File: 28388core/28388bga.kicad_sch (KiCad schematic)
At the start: 130 parts, among them IC1 F28388DZWTS, IC2 TPS62420DRCT, IC6 OPA4350EA_250, IC7 TPS3702CX33DDCT, IC8 CDCLVC1104PW, IC9 TPS3702CX12DDCT, J9 Conn_02x07_Odd_Even, Q1 FMMT618TA, Q11 AT24C16C-SSHM-T, Q2 FMMT618TA, Q4 FMMT618TA, Q46 TYPEC-304-ACP16, Q7 FMMT618TA, SW1 SW_DIP_x02, SW2 SW_Push, U1 ADR423ARMZ, Y1 ECS-2520S33-250-FN-TR

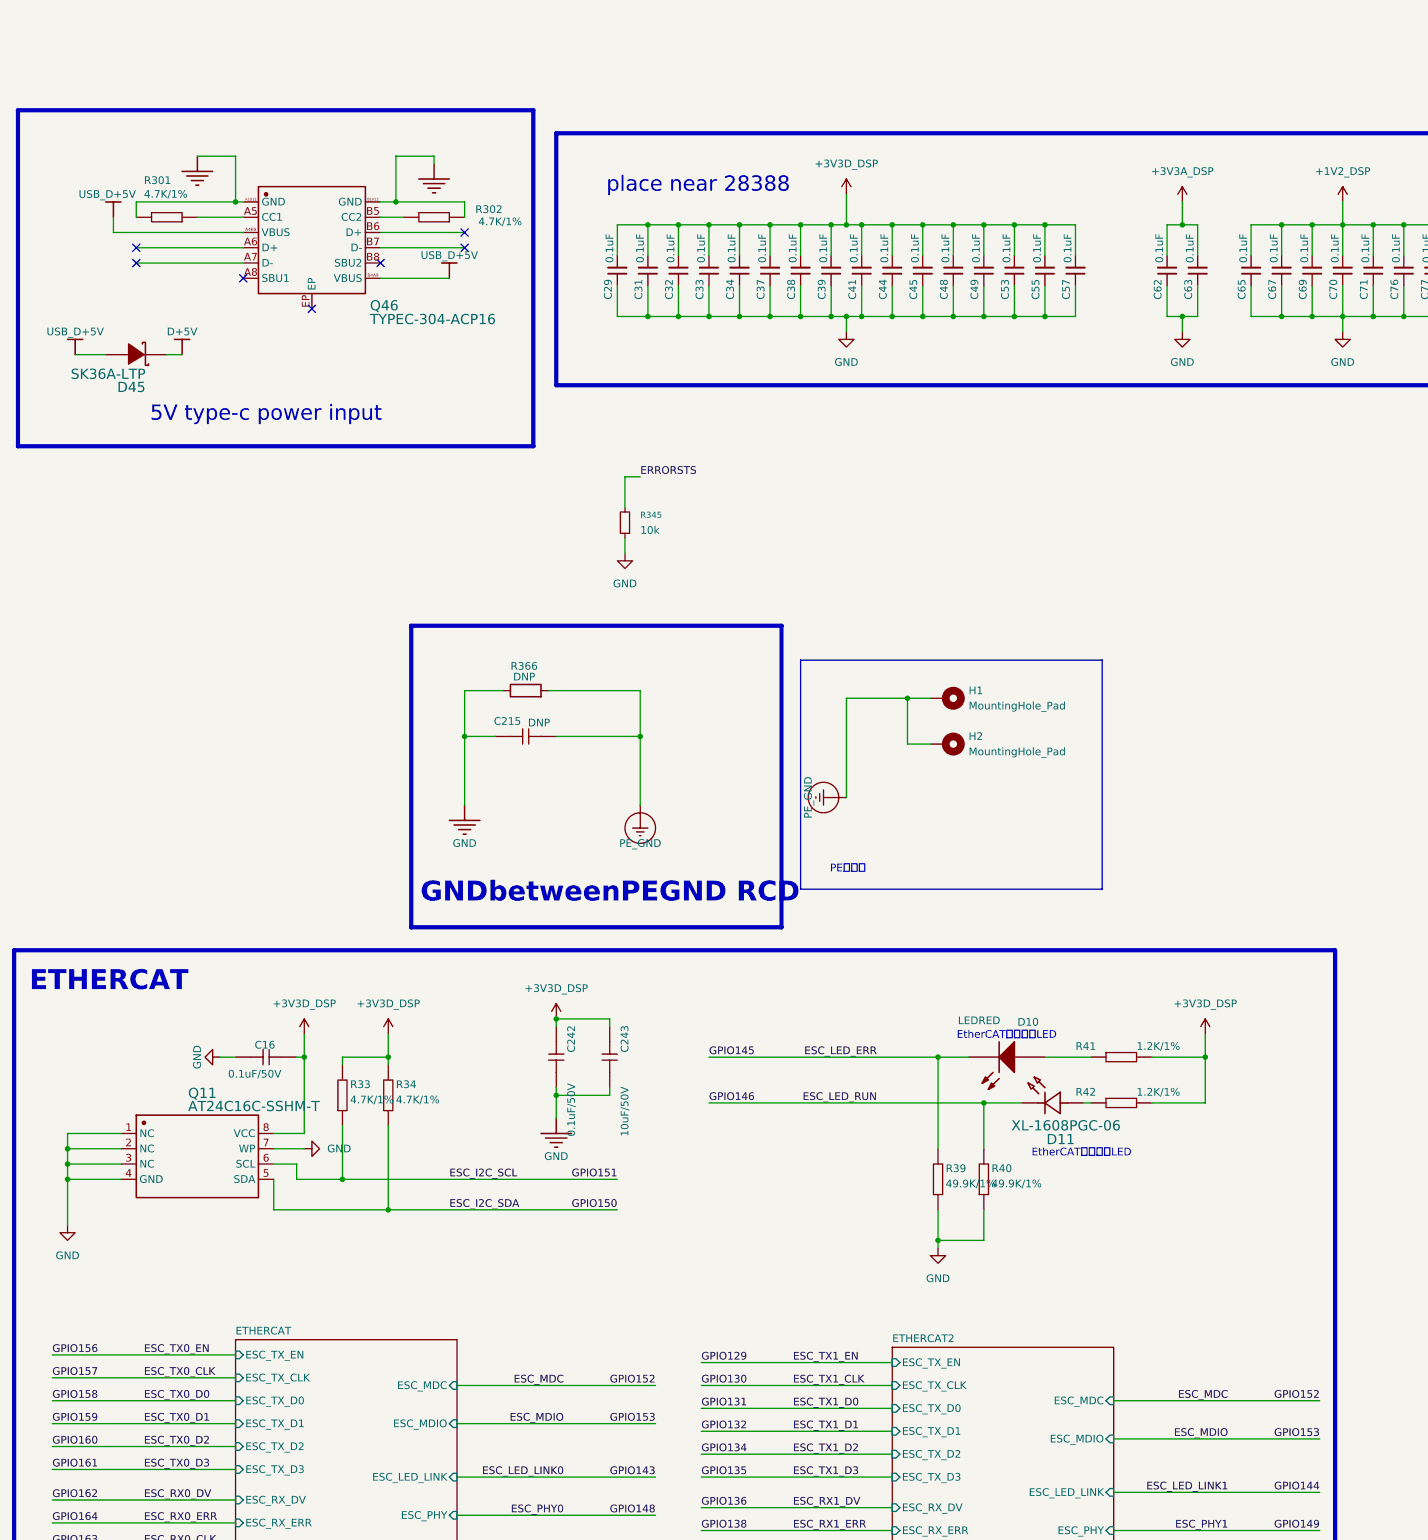
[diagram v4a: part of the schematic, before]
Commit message: 1. usb 稳压、防倒灌 1 2. 仿真器贴片 1 3. EtherCAT确认 1 4. EtherCAT差分信号 5. 金手指选型换1.6 要不就1.0？
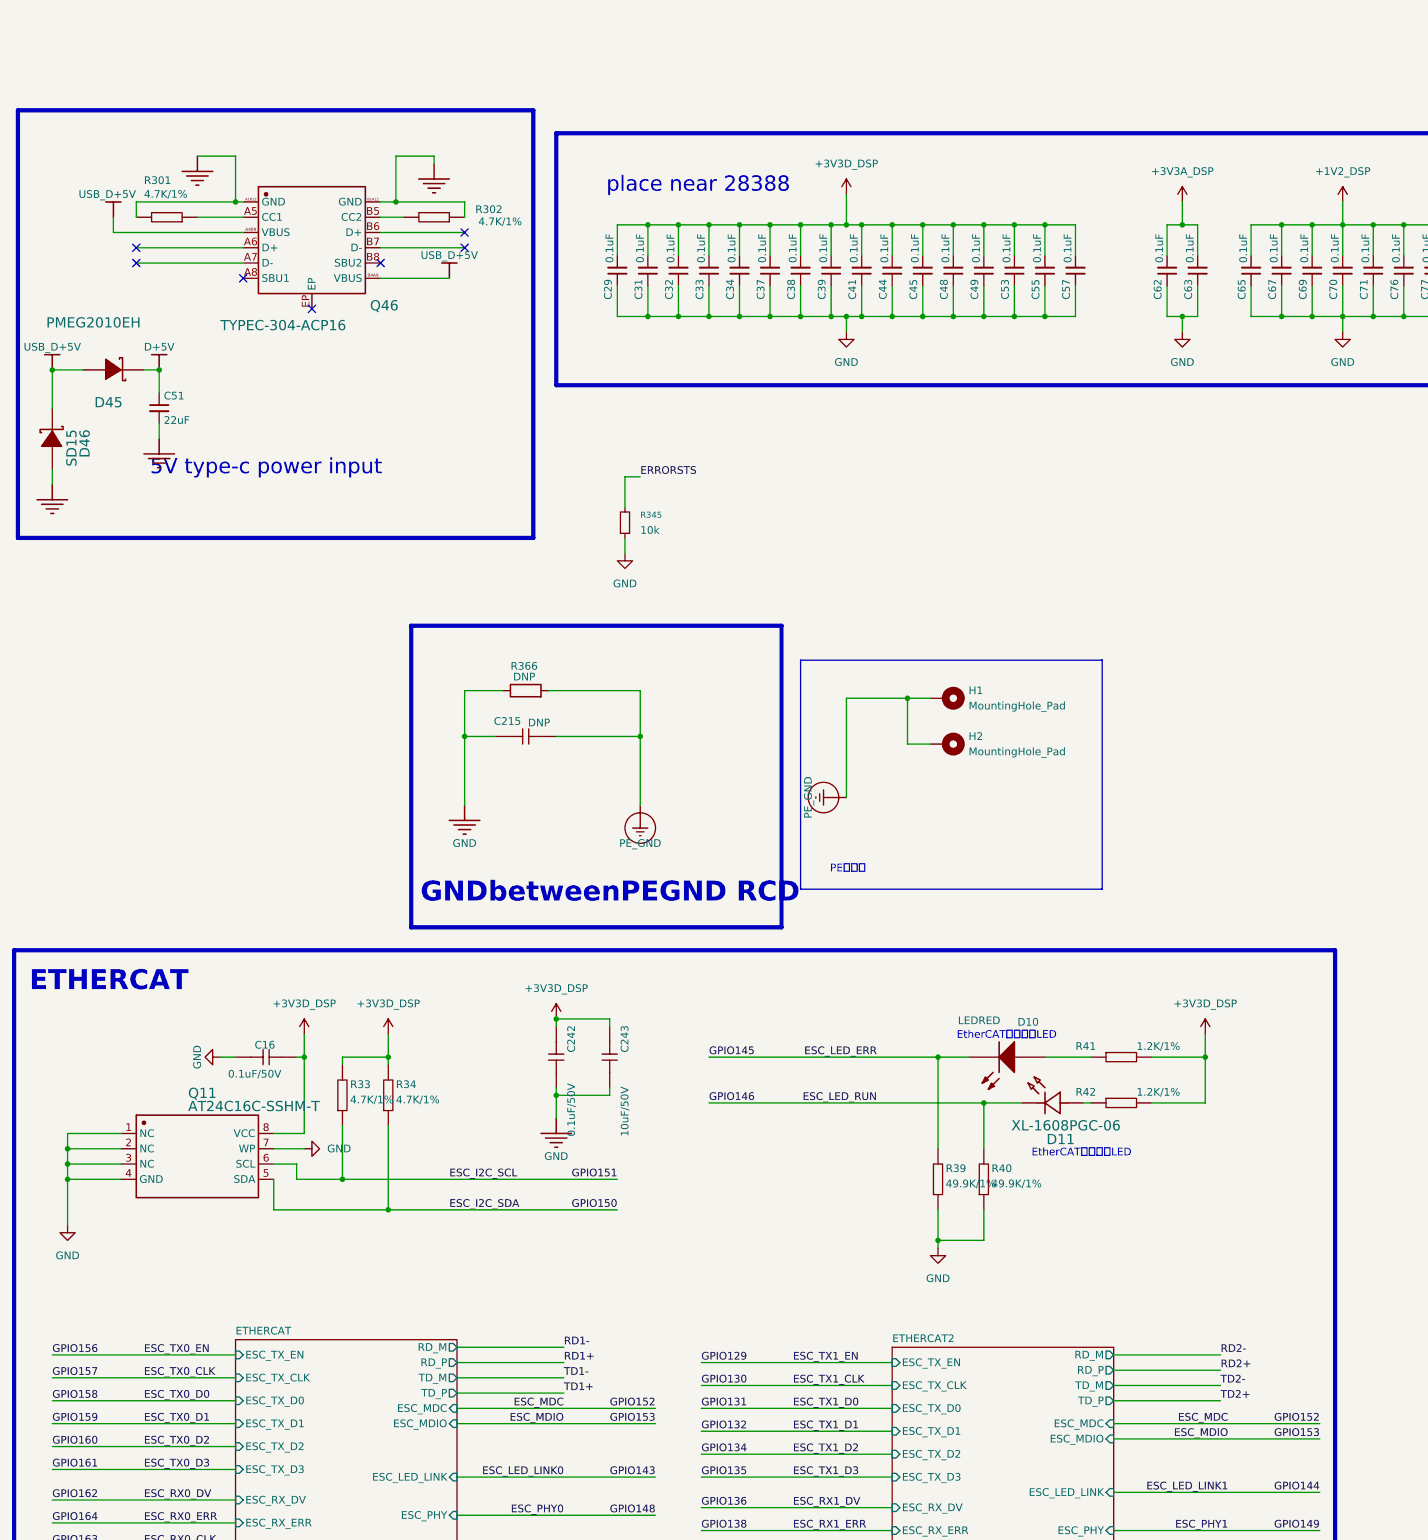
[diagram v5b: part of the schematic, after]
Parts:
- added C51: 22uF, Capacitor_SMD:C_0402_1005Metric, symbol Device:C_Small
- added D46: SD15, Diode_SMD:D_SOD-323, symbol sheet1-altium-import:SK36A-LTP
- D45: value SK36A-LTP -> PMEG2010EH; footprint Lib_sheet_10:SMA_L4.3-W2.6-LS5.2-RD -> Diode_SMD:D_SOD-123F; Manufacturer MCC(美微科) -> (none); Manufacturer Part SK36A-LTP -> (none); Supplier Part C106867 -> C552825
- J9: footprint Connector_IDC:IDC-Header_2x07_P2.54mm_Vertical -> Connector_PinHeader_2.54mm:PinHeader_2x07_P2.54mm_Vertical_SMD
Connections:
- net AGND: now also C51.2, D46.2 (A)
- net D+5V: now also C51.1
- net USB_D+5V: now also D46.1 (K)
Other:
- sheet ETHERCAT ports: added RD_M, RD_P, TD_M, TD_P; removed none
- sheet ETHERCAT2 ports: added RD_M, RD_P, TD_M, TD_P; removed none
- moved on the sheet: D45

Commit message: 使用100PIN连接器，试着重新分配引脚
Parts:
- removed CARD2: DDR3, 1mmlab_footprint:PCBComponent_1 - duplicate, symbol 1mmlab:DDR3
- added CN1, CN2: ~, 1mmlab_footprint:CONN-SMD_DF40C-100DS-0.4V-51, symbol 1mmlab:DF40C-100DS-0.4V(51)
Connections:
- net ADC_14_IN: now also CN1.90
- net ADC_15_IN: now also CN1.89
- net ADC_A0_IN: now also CN1.2
- net ADC_A1_IN: now also CN1.3
- net ADC_A2_IN: now also CN1.5
- net ADC_A3_IN: now also CN1.6
- net ADC_A4_IN: now also CN1.8
- net ADC_A5_IN: now also CN1.9
- net ADC_B0_IN: now also CN1.99
- net ADC_B1_IN: now also CN1.98
- net ADC_B2_IN: now also CN1.96
- net ADC_B3_IN: now also CN1.95
- net ADC_B4_IN: now also CN1.11
- net ADC_B5_IN: now also CN1.12
- net ADC_C2_IN: now also CN1.93
- net ADC_C3_IN: now also CN1.92
- net ADC_C4_IN: now also CN1.14
- net ADC_C5_IN: now also CN1.15
- net ADC_D0_IN: now also CN1.87
- net ADC_D1_IN: now also CN1.86
- net ADC_D2_IN: now also CN1.17
- net ADC_D3_IN: now also CN1.18
- net ADC_D4_IN: now also CN1.84
- net ADC_D5_IN: now also CN1.83
- net D+5V: now also CN1.54, CN1.61, CN1.68, CN2.100, CN2.96
- net GND: now also CN1.1, CN1.10, CN1.100, CN1.13, CN1.16, CN1.19, CN1.22, CN1.26, CN1.33, CN1.4, CN1.40, CN1.47, CN1.50, CN1.51, CN1.7, CN1.75, CN1.79, CN1.82, CN1.85, CN1.88, CN1.91, CN1.94, CN1.97, CN2.1, CN2.12, CN2.5
- net GPIO10: now also CN2.90
- net GPIO100: now also CN2.2
- net GPIO101: now also CN2.93
- net GPIO103: now also CN2.97
- net GPIO104: now also CN2.94
- net GPIO106: now also CN1.25
- net GPIO107: now also CN1.77
- net GPIO109: now also CN1.23
- net GPIO11: now also CN2.8
- net GPIO110: now also CN1.24
- net GPIO111: now also CN1.76
- net GPIO112: now also CN1.78
- net GPIO115: now also CN1.69
- net GPIO116: now also CN1.30
- net GPIO117: now also CN1.34
- net GPIO119: now also CN1.65
- net GPIO12: now also CN2.91
- net GPIO120: now also CN1.37
- net GPIO121: now also CN1.38
- net GPIO122: now also CN1.27
- net GPIO123: now also CN1.28
- net GPIO124: now also CN1.29
- net GPIO126: now also CN1.74
- net GPIO127: now also CN1.73
- net GPIO128: now also CN1.72
- net GPIO13: now also CN2.7
- net GPIO14: now also CN2.92
- net GPIO16: now also CN2.6
- net GPIO17: now also CN2.11
- net GPIO20: now also CN2.10
- net GPIO24: now also CN2.14
- net GPIO25: now also CN2.95
- net GPIO26: now also CN2.99
- net GPIO27: now also CN2.98
- net GPIO28: now also CN1.31
- net GPIO29: now also CN1.32
- net GPIO30: now also CN1.71
- net GPIO31: now also CN1.70
- net GPIO32: now also CN1.35
- net GPIO33: now also CN1.36
- net GPIO34: now also CN1.67
- net GPIO35: now also CN1.66
- net GPIO36: now also CN1.39
- net GPIO37: now also CN1.64
- net GPIO38: now also CN1.63
- net GPIO39: now also CN1.60
- net GPIO40: now also CN1.59
- net GPIO41: now also CN1.58
- net GPIO48: now also CN1.62
- net GPIO49: now also CN1.44
- net GPIO50: now also CN1.56
- net GPIO51: now also CN1.53
- net GPIO52: now also CN1.41
- net GPIO53: now also CN1.45
- net GPIO54: now also CN1.55
- net GPIO55: now also CN1.49
- net GPIO56: now also CN1.42
- net GPIO57: now also CN1.48
- net GPIO58: now also CN1.46
- net GPIO59: now also CN1.43
- net GPIO60: now also CN1.57
- net GPIO8: now also CN2.9
- net GPIO97: now also CN2.13
- net GPIO98: now also CN2.3
- net GPIO99: now also CN2.4
- no-connect marks 27 -> 24
